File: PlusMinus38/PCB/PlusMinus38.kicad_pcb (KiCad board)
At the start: 2 copper layers, 98.2 x 84.1 mm, 42 parts

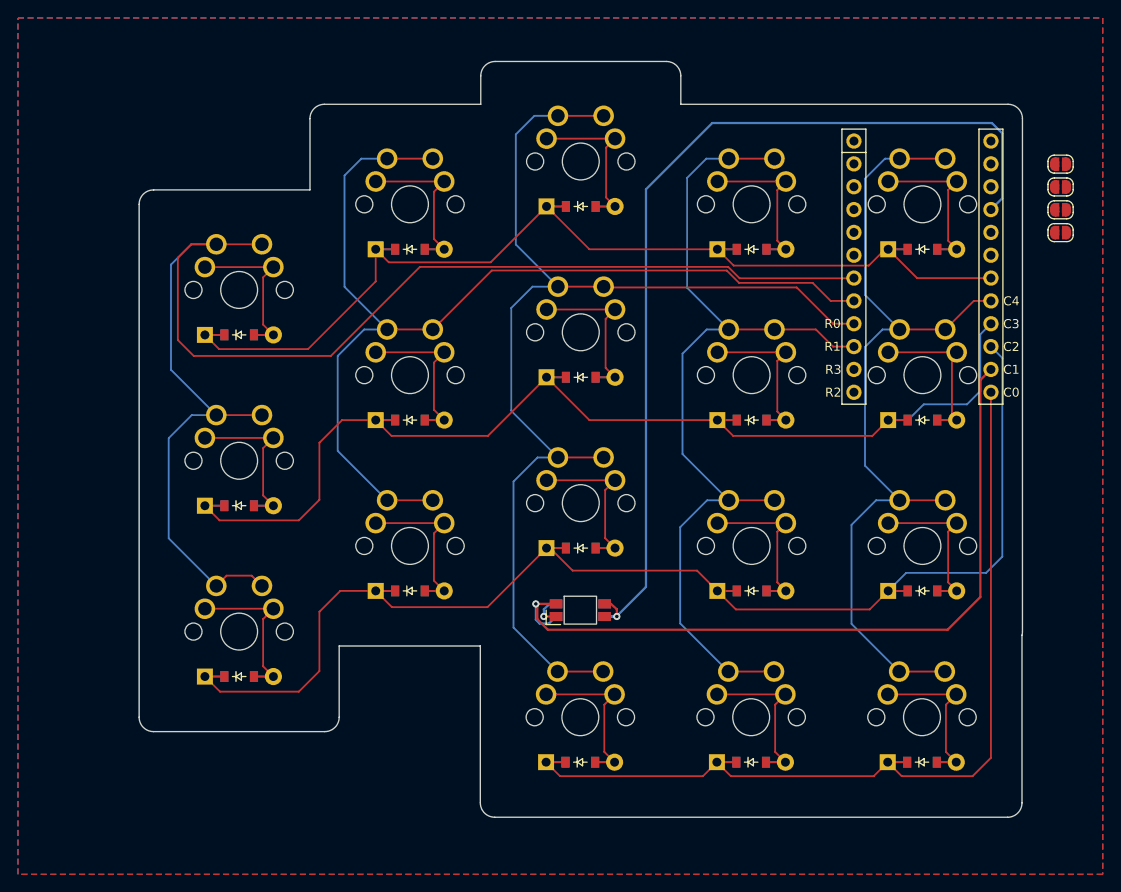
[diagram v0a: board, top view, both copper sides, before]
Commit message: Added solderjumpers to reverse the keyboard
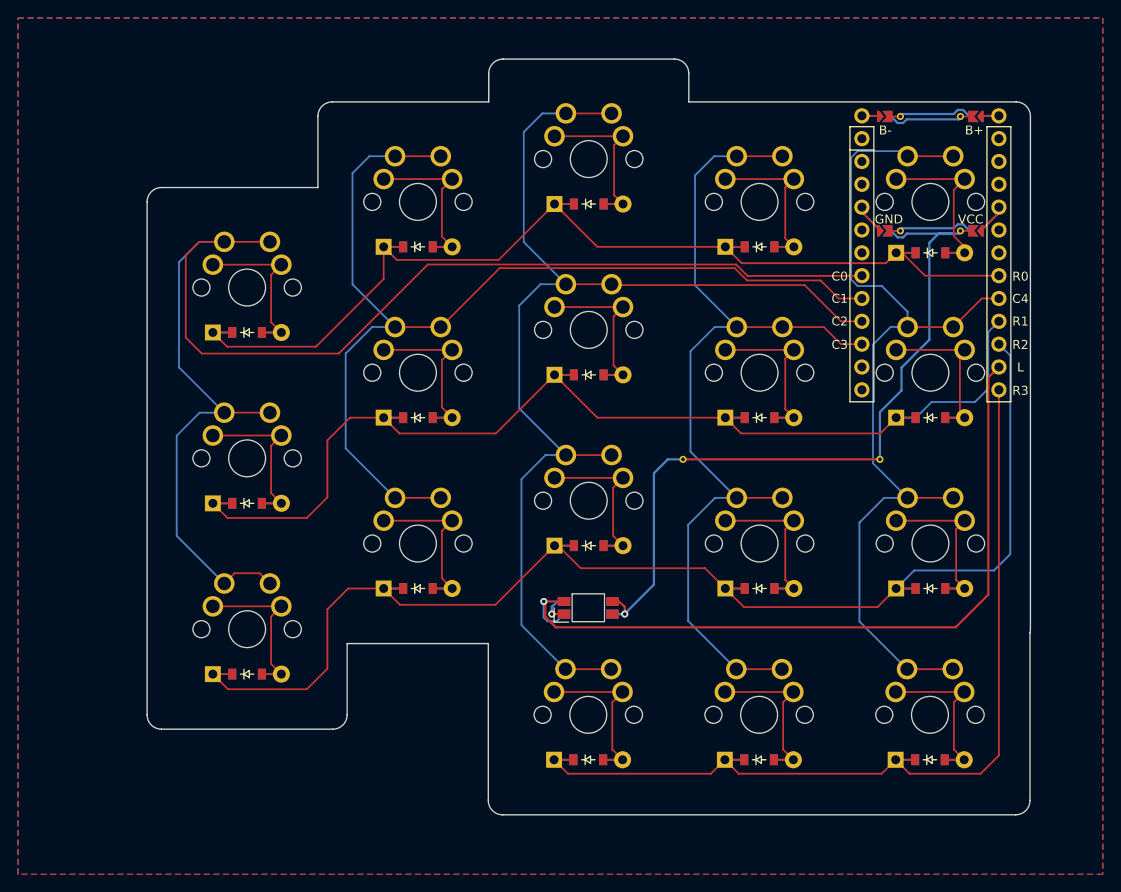
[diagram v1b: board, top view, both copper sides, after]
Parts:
- removed REF** (x4): SolderJumper-2_P1.3mm_Open_RoundedPad1.0x1.5mm, Jumper:SolderJumper-2_P1.3mm_Open_RoundedPad1.0x1.5mm
- added ?: , , F.Cu at (121.3, 80.8)
- added ?: , , F.Cu at (123.5, 42.7)
- added ?: , , F.Cu at (130.2, 55.4)
- added ?: , , F.Cu at (122.2, 42.7)
- added ?: , , F.Cu at (131.6, 55.4)
- added ?: , , F.Cu at (119.3, 42.6)
- added ?: , , F.Cu at (121.4, 55.4)
- added ?: , , F.Cu at (121.4, 42.7)
- added ?: , , B.Cu at (132.3, 55.4)
- added ?: , , B.Cu at (131.6, 55.4)
- added ?: , , B.Cu at (122.2, 42.7)
- added ?: , , F.Cu at (130.2, 42.7)
- added ?: , , B.Cu at (122.2, 55.4)
- added ?: , , B.Cu at (121.4, 55.4)
- added ?: , , B.Cu at (132.3, 42.7)
- added ?: , , B.Cu at (131.6, 42.7)
- added ?: , , B.Cu at (121.4, 42.7)
- added ?: , , F.Cu at (131.6, 42.7)
- added ?: , , F.Cu at (132.3, 55.4)
- added ?: , , F.Cu at (123.5, 55.4)
- added ?: , , F.Cu at (134.5, 42.5)
- added ?: , , F.Cu at (122.2, 55.4)
- added ?: , , F.Cu at (132.3, 42.7)
- added ?: , , F.Cu at (99.4, 80.8)
- moved D15 0.97 mm to (126.9, 57.9)
- moved D1 0.93 mm to (50.9, 104.7)
- moved D2 0.93 mm to (50.9, 85.7)
- moved D3 0.93 mm to (50.9, 66.7)
- moved S1 0.93 mm to (50.9, 99.7)
- moved S2 0.93 mm to (50.9, 80.7)
- moved S3 0.93 mm to (50.9, 61.7)
- moved D12 0.93 mm to (107.9, 57.2)
- moved D16 0.93 mm to (88.8, 114.3)
- moved D17 0.93 mm to (107.8, 114.3)
- moved D18 0.93 mm to (126.8, 114.3)
- moved D6 0.93 mm to (69.9, 57.2)
- moved D7 0.93 mm to (88.9, 90.4)
- moved D8 0.93 mm to (88.9, 71.4)
- moved LED1 0.93 mm to (88.8, 97.4)
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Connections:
- MCU1 pad 1: RAW -> (no net)
- MCU1 pad 19: P3 -> (no net)
- MCU1 pad 2: GND -> (no net)
- MCU1 pad 20: P2 -> (no net)
- MCU1 pad 21: GND -> G_SEL
- MCU1 pad 22: GND -> (no net)
- MCU1 pad 23: P0 -> (no net)
- MCU1 pad 24: P1 -> (no net)
- MCU1 pad 3: RST -> (no net)
- MCU1 pad 4: VCC -> V_SEL
- MCU1 pad 5: P21 -> (no net)
- MCU1 pad 6: P20 -> (no net)
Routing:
- net VCC: track 106.1 -> 87.3 mm
- net GND: track 3.75 -> 13.6 mm
- net B-: track 0.00 -> 9.84 mm
- net B+: track 0.00 -> 9.84 mm
- net G_SEL: track 0.00 -> 7.19 mm
- net V_SEL: track 0.00 -> 7.08 mm
- net C4: track 98.1 -> 104.8 mm
- net POW+: track 0.00 -> 4.42 mm
- net POW-: track 0.00 -> 4.42 mm
- net R0: track 124.5 -> 123.6 mm
- net inner_top: track 20.3 -> 21.1 mm
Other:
- outline, holes or cut-outs redrawn
- board text added: "B+"
- board text added: "B-"
- board text added: "C0"
- board text added: "C1"
- board text added: "C2"
- board text added: "C3"
- board text added: "C4"
- board text added: "GND"
- board text added: "L"
- board text added: "R0"
- board text added: "R1"
- board text added: "R2"
- board text added: "R3"
- board text added: "VCC"

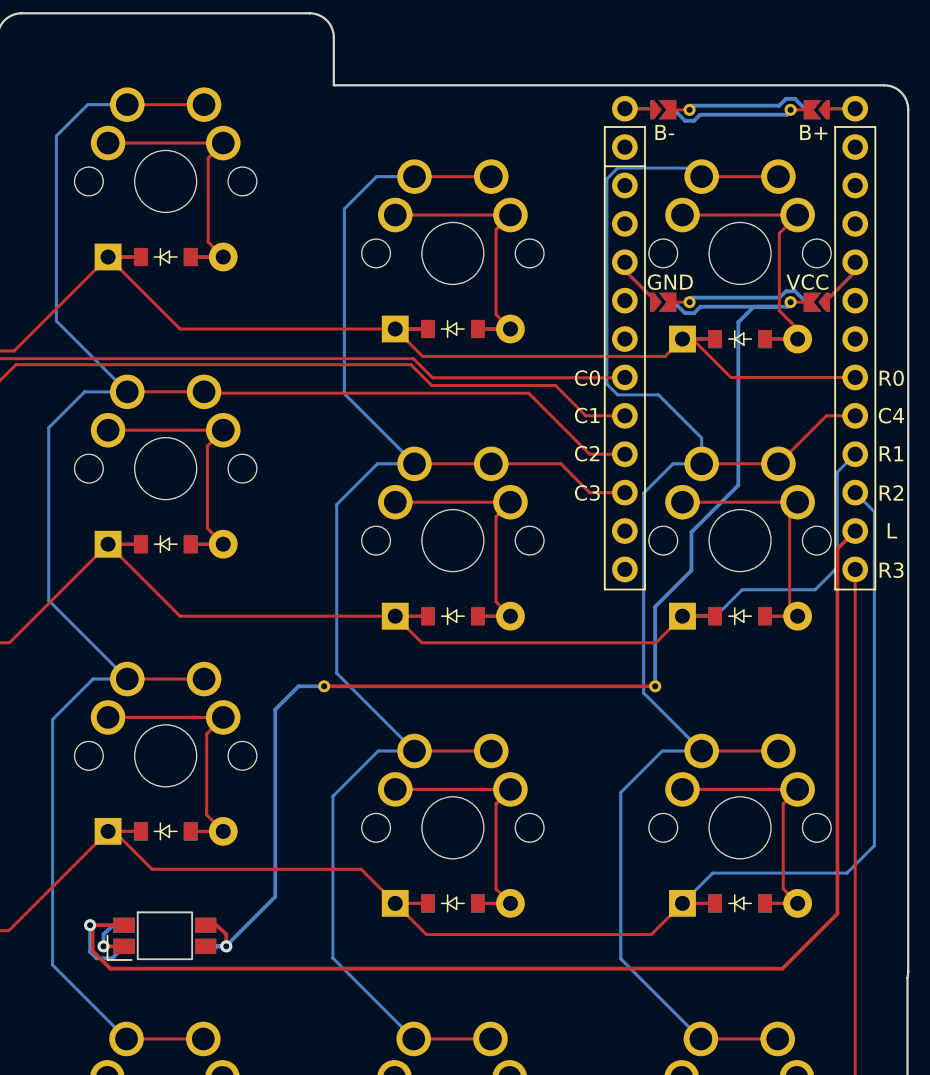
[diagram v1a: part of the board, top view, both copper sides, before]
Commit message: Fixed reverse solder pads traces. Updated ergogen yaml to match pcb
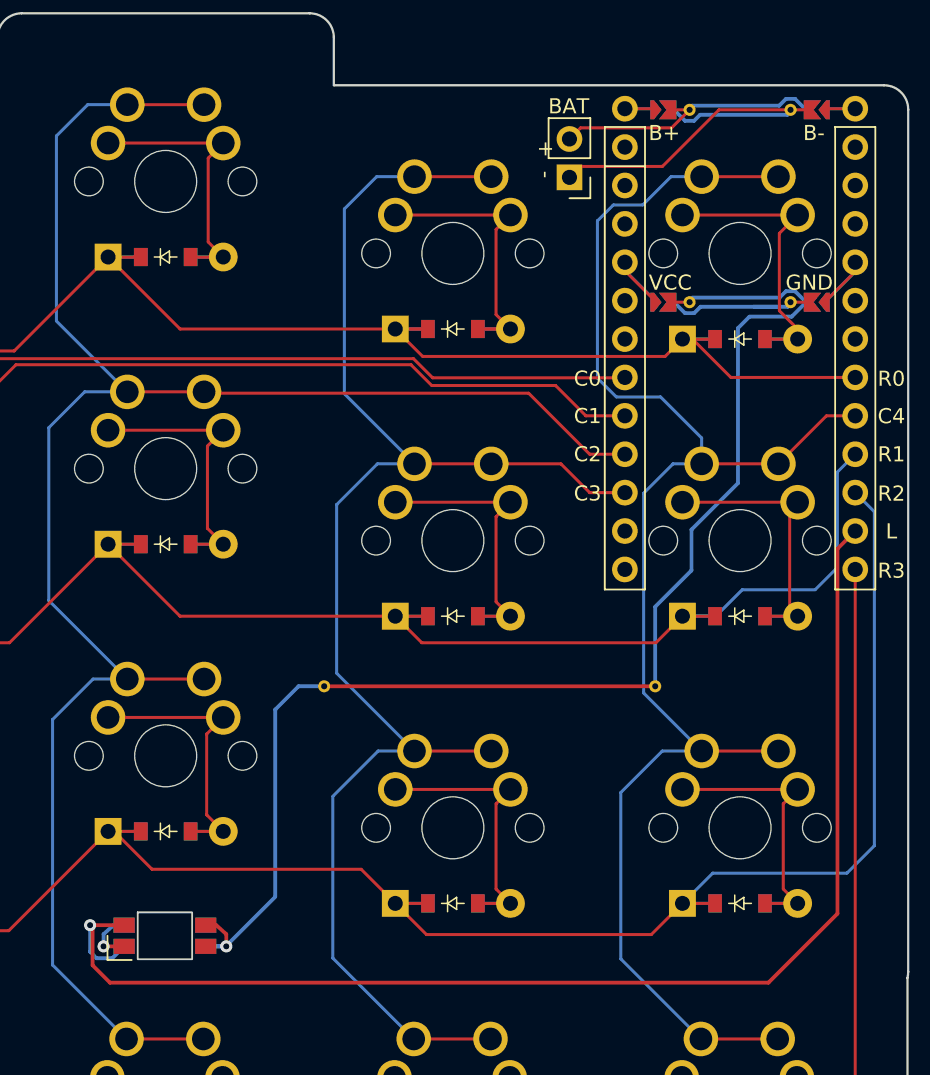
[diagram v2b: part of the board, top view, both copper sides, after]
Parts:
- added BAT: PinHeader_1x02_P2.54mm_Vertical, Connector_PinHeader_2.54mm:PinHeader_1x02_P2.54mm_Vertical, F.Cu at (115.6, 47.2)
- S15: moved to F.Cu
- turned S15 to 180 degrees
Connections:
- ? pad 124: B- -> B+ (x2)
- ? pad 124: VCC -> GND (x2)
- ? pad 101: GND -> VCC
- ? pad 101: B+ -> B-
- ? pad 124: B+ -> B- (x2)
- ? pad 101: VCC -> GND
- ? pad 101: B- -> B+
- ? pad 124: GND -> VCC (x2)
- MCU1 pad 13: P9 -> (no net)
- MCU1 pad 14: P8 -> (no net)
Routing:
- net B-: track 9.84 -> 26.3 mm
- net B+: track 9.84 -> 18.6 mm
- net VCC: track 87.3 -> 89.3 mm
- net GND: track 13.6 -> 15.3 mm
- net LED: track 85.6 -> 86.9 mm
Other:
- board text added: "+ -"

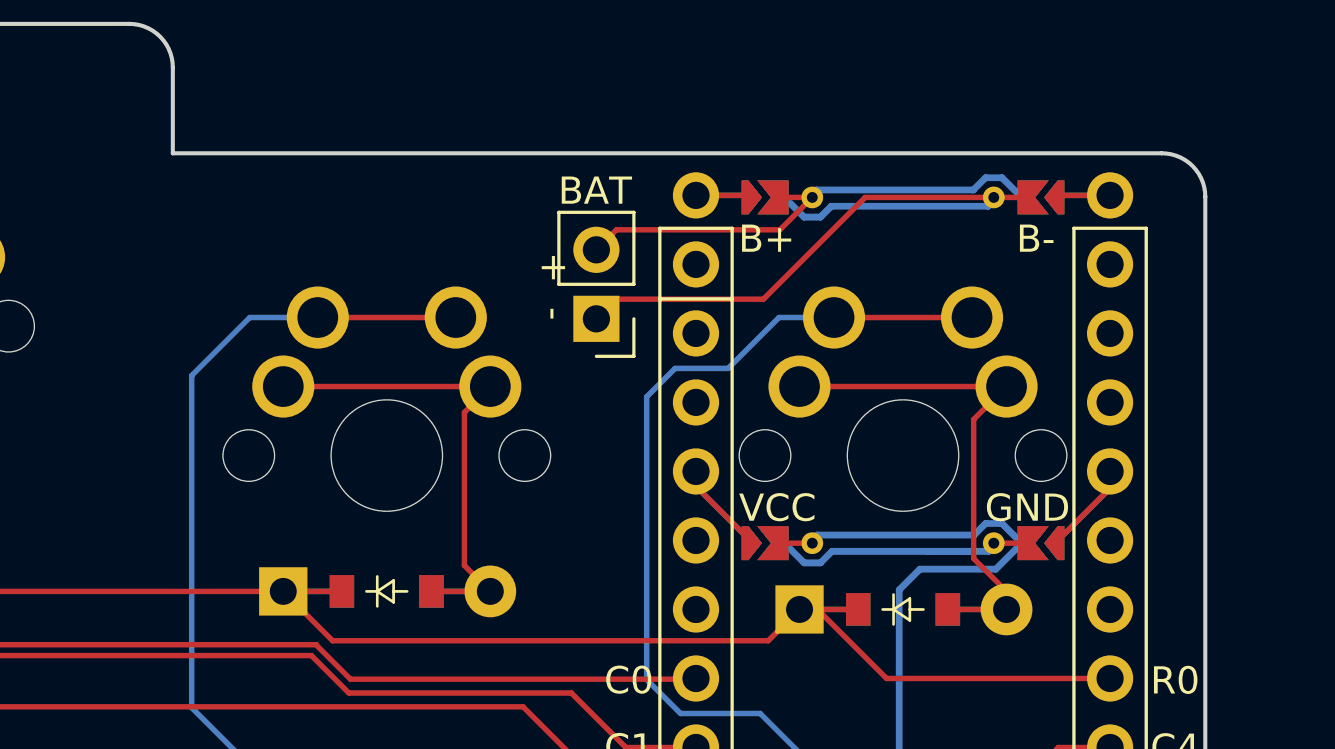
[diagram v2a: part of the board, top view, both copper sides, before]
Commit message: Added power switch
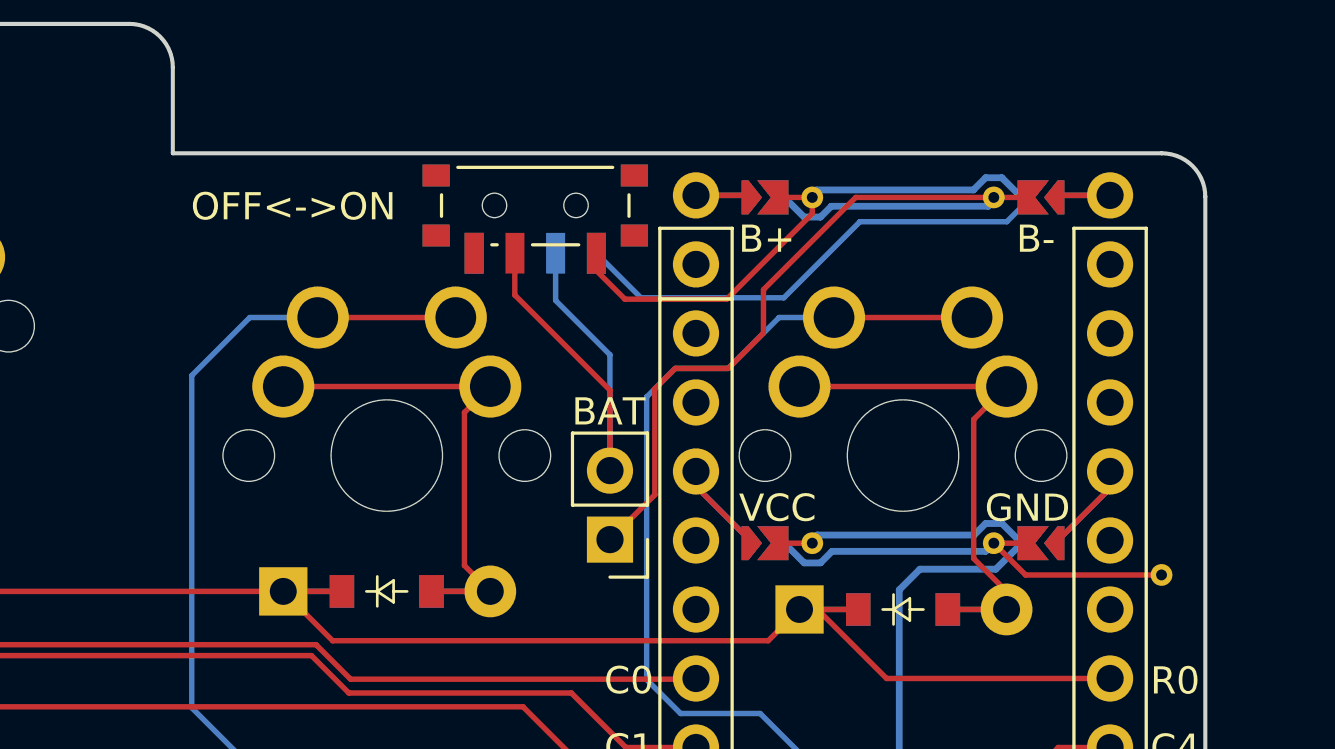
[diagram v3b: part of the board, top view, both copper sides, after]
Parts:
- added ?: , , F.Cu at (136.4, 56.6)
- added PWR1: , ceoloide:power_switch_smd_side, F.Cu at (113.3, 43.0)
- moved BAT 8.14 mm to (116.1, 55.3)
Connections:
- BAT pad 2: B+ -> PWR+
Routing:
- net B+: track 18.6 -> 39.0 mm
- net PWR+: track 0.00 -> 18.3 mm
- net B-: track 26.3 -> 32.4 mm
- net GND: track 15.3 -> 20.4 mm
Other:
- board text added: "+"
- board text added: "-"
- board text removed: "+ -"

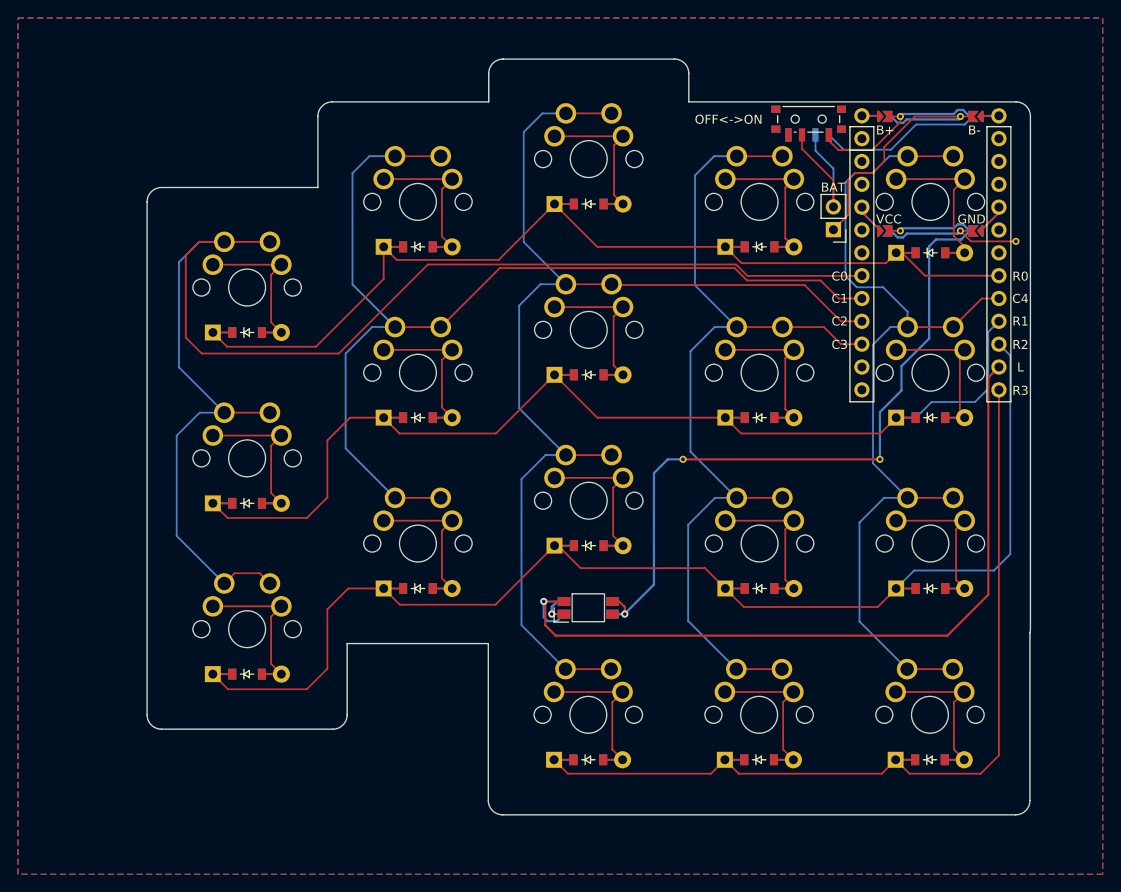
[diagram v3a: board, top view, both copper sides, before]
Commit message: Added leds to the rgb chain
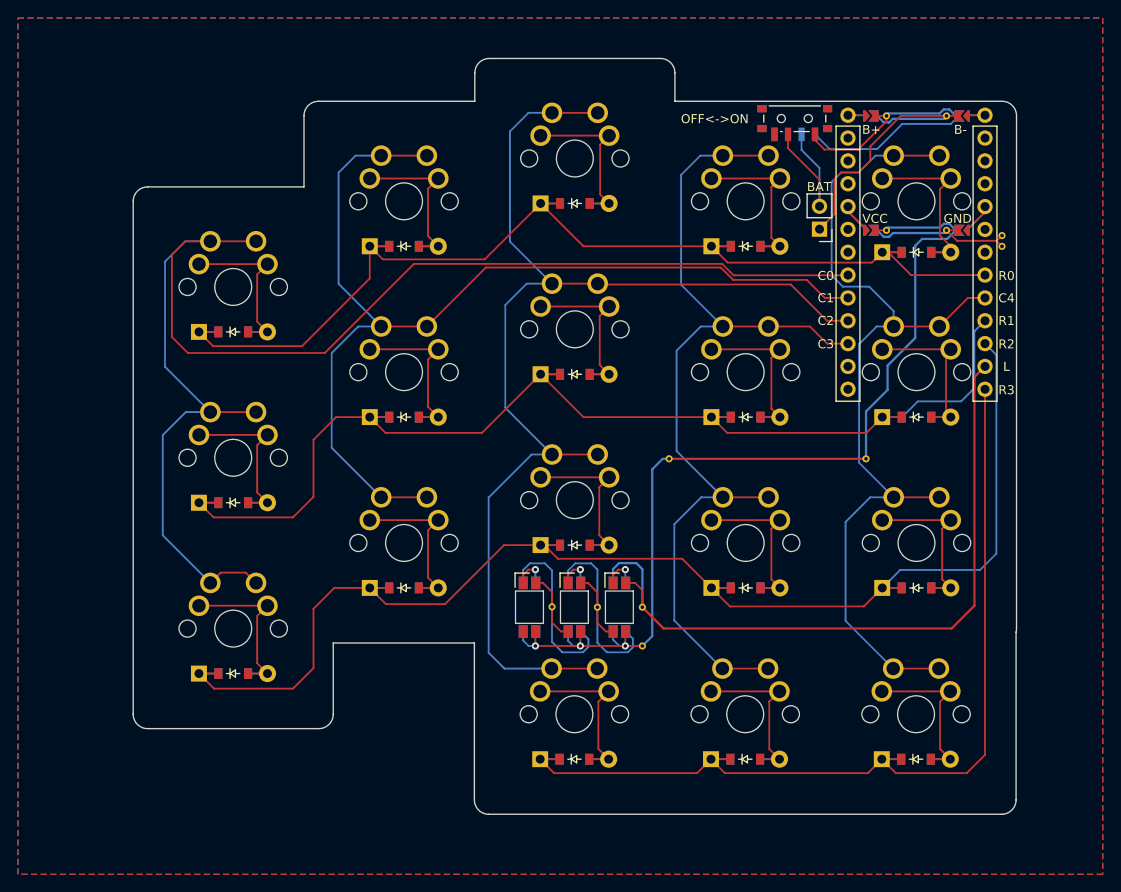
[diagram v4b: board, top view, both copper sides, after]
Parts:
- added ?: , , F.Cu at (89.8, 97.3)
- added ?: , , F.Cu at (84.8, 97.2)
- added ?: , , F.Cu at (94.8, 101.6)
- added ?: , , F.Cu at (94.8, 97.3)
- added ?: , , F.Cu at (134.8, 57.1)
- added LED1: , ceoloide:led_SK6812mini-e (per-key, reversible), B.Cu at (82.3, 97.3)
- added LED1: , ceoloide:led_SK6812mini-e (per-key, reversible), B.Cu at (87.3, 97.3)
- moved LED1 3.45 mm to (92.3, 97.3), turned to -90 degrees
- moved ? 1.68 mm to (134.9, 56.0)
- moved ? 1.55 mm to (97.8, 80.8)
- moved ? 1.55 mm to (122.0, 42.6)
- moved ? 1.55 mm to (120.6, 42.6) (x2)
- moved ? 1.55 mm to (117.7, 42.6)
- moved ? 1.55 mm to (120.6, 55.4) (x2)
- moved ? 1.55 mm to (122.0, 55.4)
- moved S3 1.55 mm to (49.3, 61.7)
- moved D1 1.55 mm to (49.3, 104.7)
- moved D2 1.55 mm to (49.3, 85.7)
- moved D3 1.55 mm to (49.3, 66.7)
- moved S1 1.55 mm to (49.3, 99.7)
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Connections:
- net LED renamed LED_0_IN
- LED1 pad 2: (no net) -> LED_0_OUT
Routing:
- net LED_0_OUT: track 0.00 -> 27.9 mm
- net LED_1_OUT: track 0.00 -> 27.9 mm
- net VCC: track 89.3 -> 110.4 mm, vias 1 -> 3
- net GND: track 20.4 -> 29.8 mm, vias 1 -> 3
- net LED_0_IN: track 86.9 -> 79.7 mm, vias 1 -> 0
- net C2: track 128.5 -> 133.3 mm
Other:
- outline, holes or cut-outs redrawn

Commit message: Fliped the solder jumpers for better access
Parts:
- added ?: , , F.Cu at (114.0, 46.4)
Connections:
- ? pad 124: VCC -> GND (x2)
- ? pad 124: B+ -> B- (x2)
- ? pad 124: GND -> VCC (x2)
- ? pad 101: VCC -> GND
- ? pad 101: B- -> B+
- ? pad 101: GND -> VCC
- ? pad 101: B+ -> B-
- ? pad 124: B- -> B+ (x2)
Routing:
- net B+: track 39.0 -> 29.6 mm
- net B-: track 32.4 -> 26.5 mm
- net GND: track 29.8 -> 28.9 mm
- net VCC: track 110.4 -> 109.5 mm
